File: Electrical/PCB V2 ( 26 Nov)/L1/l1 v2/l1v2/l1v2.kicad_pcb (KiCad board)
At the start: 2 copper layers, 177.9 x 169.6 mm, 194 parts, among them J1 Conn_01x01_Socket, J2 Conn_01x01_Socket, J3 Conn_01x02, SW1 SW_SPDT, U1 102010428, U2 CD74HC4067SM, U3 CD74HC4067SM, U4 XT30UPB-M

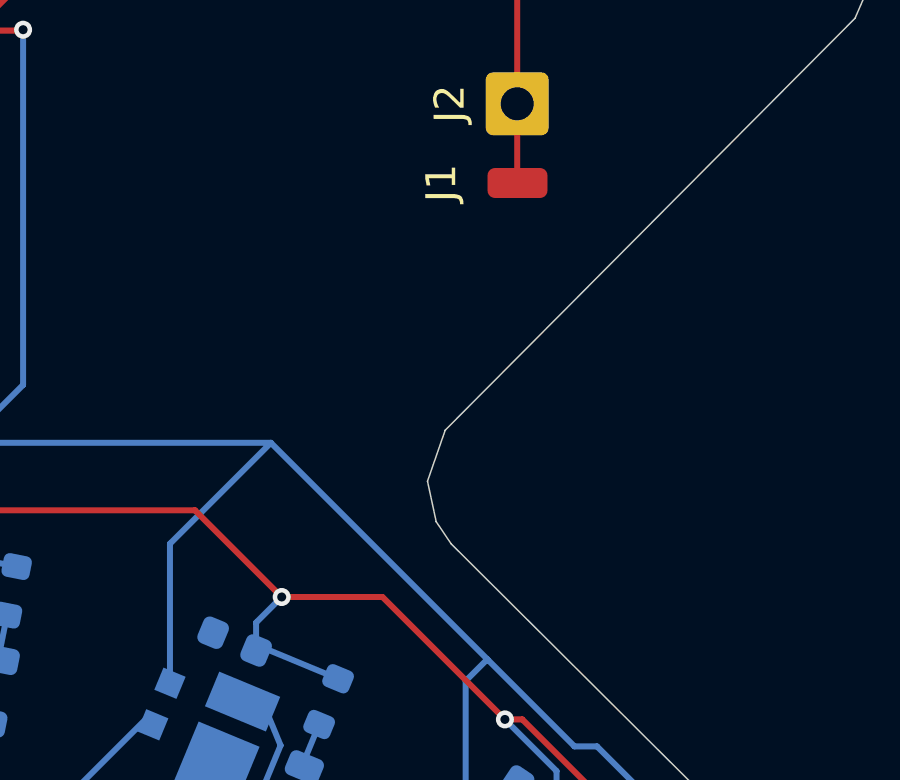
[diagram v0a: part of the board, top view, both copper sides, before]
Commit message: changed some stuff for l1, uploaded updated l2 layout
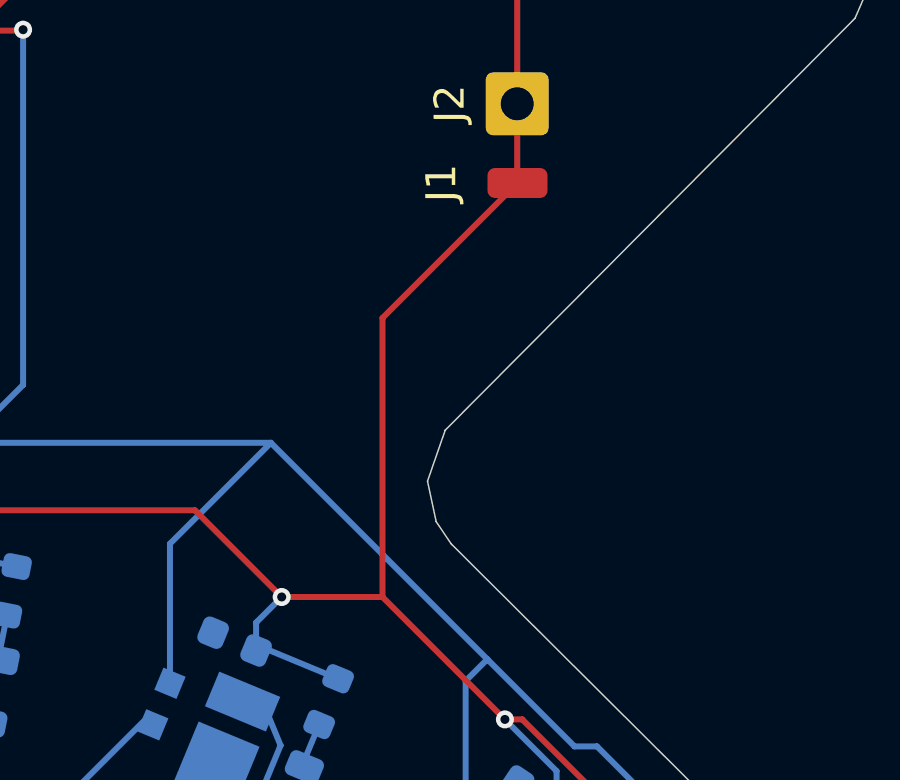
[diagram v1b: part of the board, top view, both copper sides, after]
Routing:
- net pwr for photoresistors: track 620.7 -> 636.4 mm
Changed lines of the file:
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@@
 		(fp_arc
 			(start 8.800012 9.000008)
-			(mid 7.977244 10.068139)
+			(mid 7.977245 10.06814)
 			(end 6.700004 10.500001)
 			(stroke
@@
 		(fp_arc
 			(start 6.700002 -10.5)
-			(mid 8.214696 -9.954473)
+			(mid 8.214693 -9.954472)
 			(end 8.899996 -8.497676)
 			(stroke
@@
 		)
 		(fp_text user "${REFERENCE}"
-			(at 0.75 -0.499999 360)
+			(at 0.75 -0.499999 0)
 			(layer "B.Fab")
 			(effects
@@
 	)
 	(segment
+		(start 148.11 39.33)
+		(end 143.61 43.83)
+		(width 0.2)
+		(layer "F.Cu")
+		(net 37)
+	)
+	(segment
 		(start 133.81 25.59)
 		(end 144.88 25.59)
@@
 	)
 	(segment
+		(start 143.61 43.83)
+		(end 143.61 53.13)
+		(width 0.2)
+		(layer "F.Cu")
+		(net 37)
+	)
+	(segment
 		(start 174.72 132.98)
 		(end 169.66 138.04)
@@
 			"c172534d-b89f-4083-b3c3-40d19f9c3ab1" "cc1ad0f2-ca86-488c-a842-2dd7c9f00347"
 			"d62ea196-b2cf-40e8-9aa5-9496fdbd3112" "dc3dc24f-7620-4e29-8b7f-fa7f0e35222d"
-			"e2f325dd-1a45-4955-ac71-bf022531d2be" "eecf311d-b65d-4bf0-9d72-7b8c42e669fd"
-			"f0b2fa90-6832-4ca1-95d8-5091ee1ed118"
+			"eecf311d-b65d-4bf0-9d72-7b8c42e669fd" "f0b2fa90-6832-4ca1-95d8-5091ee1ed118"
 		)
 	)

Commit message: did some stuff to pcb
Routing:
- net pwr for photoresistors: track 636.4 -> 633.0 mm
- net /S3: track 114.4 -> 115.5 mm

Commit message: added l2 dxf, idk what else sth about the pcb
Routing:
- net pwr for photoresistors: track 633.0 -> 630.5 mm
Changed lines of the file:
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@@
 		(fp_arc
 			(start 8.800012 9.000008)
-			(mid 7.977244 10.068136)
+			(mid 7.977245 10.06814)
 			(end 6.700004 10.500001)
 			(stroke
@@
 		)
 	)
+	(gr_arc
+		(start 155.03 65.039999)
+		(mid 151.889578 64.295934)
+		(end 152.099717 61.075418)
+		(stroke
+			(width 0.2)
+			(type default)
+		)
+		(layer "F.Cu")
+		(net 37)
+	)
 	(gr_rect
 		(start -33.05 5.11)
@@
 	)
 	(gr_text "\n2-Chairs"
+		(at 194.88 107.77 90)
+		(layer "F.SilkS")
+		(effects
+			(font
+				(size 1.5 1.5)
+				(thickness 0.3)
+				(bold yes)
+			)
+		)
+	)
+	(gr_text "\n2-Chairs"
 		(at 117.4 173.66 0)
 		(layer "F.SilkS")
@@
 		)
 	)
+	(gr_text "\n2-Chairs"
+		(at 40.65 108.76 -90)
+		(layer "F.SilkS")
+		(effects
+			(font
+				(size 1.5 1.5)
+				(thickness 0.3)
+				(bold yes)
+			)
+		)
+	)
 	(gr_text "GND"
 		(at 102.59 24.38 0)
@@
 	)
 	(segment
-		(start 148.27 57.21)
-		(end 155.55 64.49)
-		(width 0.2)
-		(layer "F.Cu")
-		(net 37)
-	)
-	(segment
 		(start 58.98 94.54)
 		(end 60.89 92.63)
@@
 		(width 0.2)
 		(layer "F.Cu")
+		(net 37)
+	)
+	(segment
+		(start 148.27 57.21)
+		(end 153.75 62.69)
+		(width 0.2)
+		(layer "F.Cu")
